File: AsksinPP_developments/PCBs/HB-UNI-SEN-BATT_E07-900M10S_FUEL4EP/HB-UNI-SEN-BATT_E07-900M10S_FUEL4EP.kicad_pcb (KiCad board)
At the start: 2 copper layers, 75 x 75 mm, 31 parts, among them J1 Conn_01x02, J10 charge, J11 ePaper connector, J2 Conn_01x02, J3 Conn_01x02, J4 Conn_01x02, J5 ISP Programmer, J6 Conn_01x04, J7 Conn_01x04, J8 Conn_01x04, J9 Conn_01x04, Q1 IRLU024N, SW1 config button

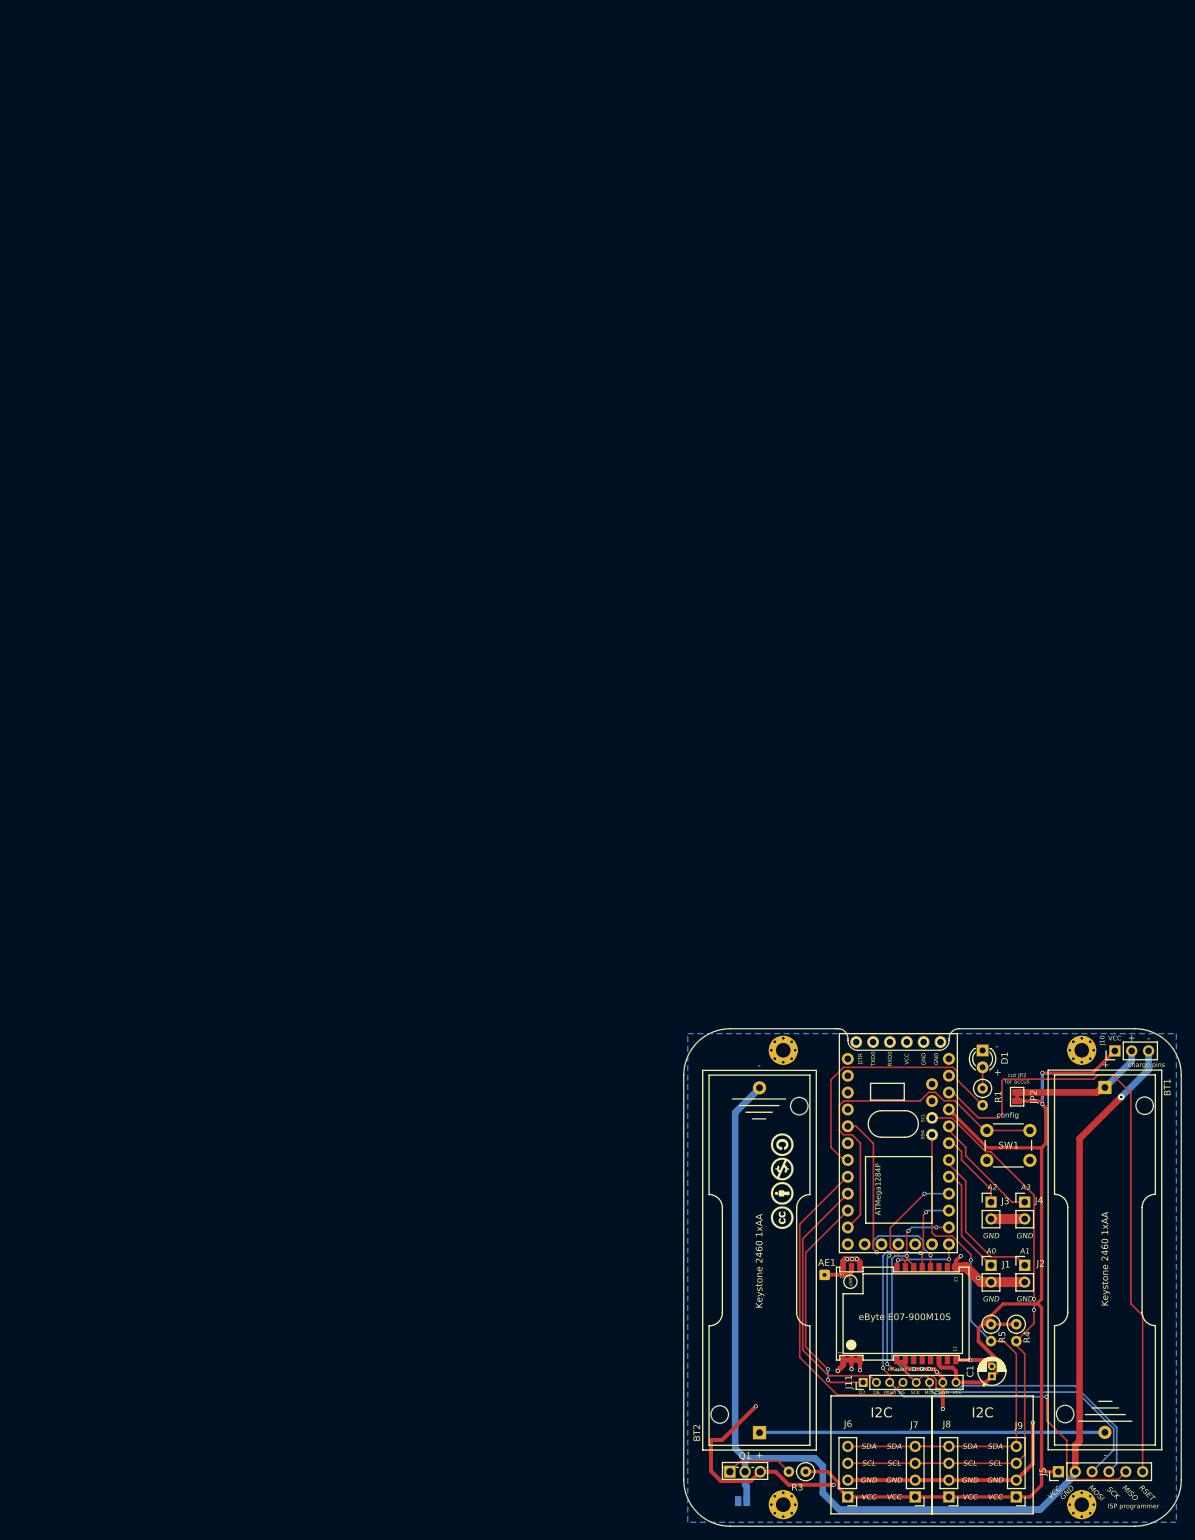
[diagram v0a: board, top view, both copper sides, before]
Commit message: PCBs: Fixes to ensure a proper production at JLCPCB, e.g. corrections of origins, rotations of assembled ICs etc.
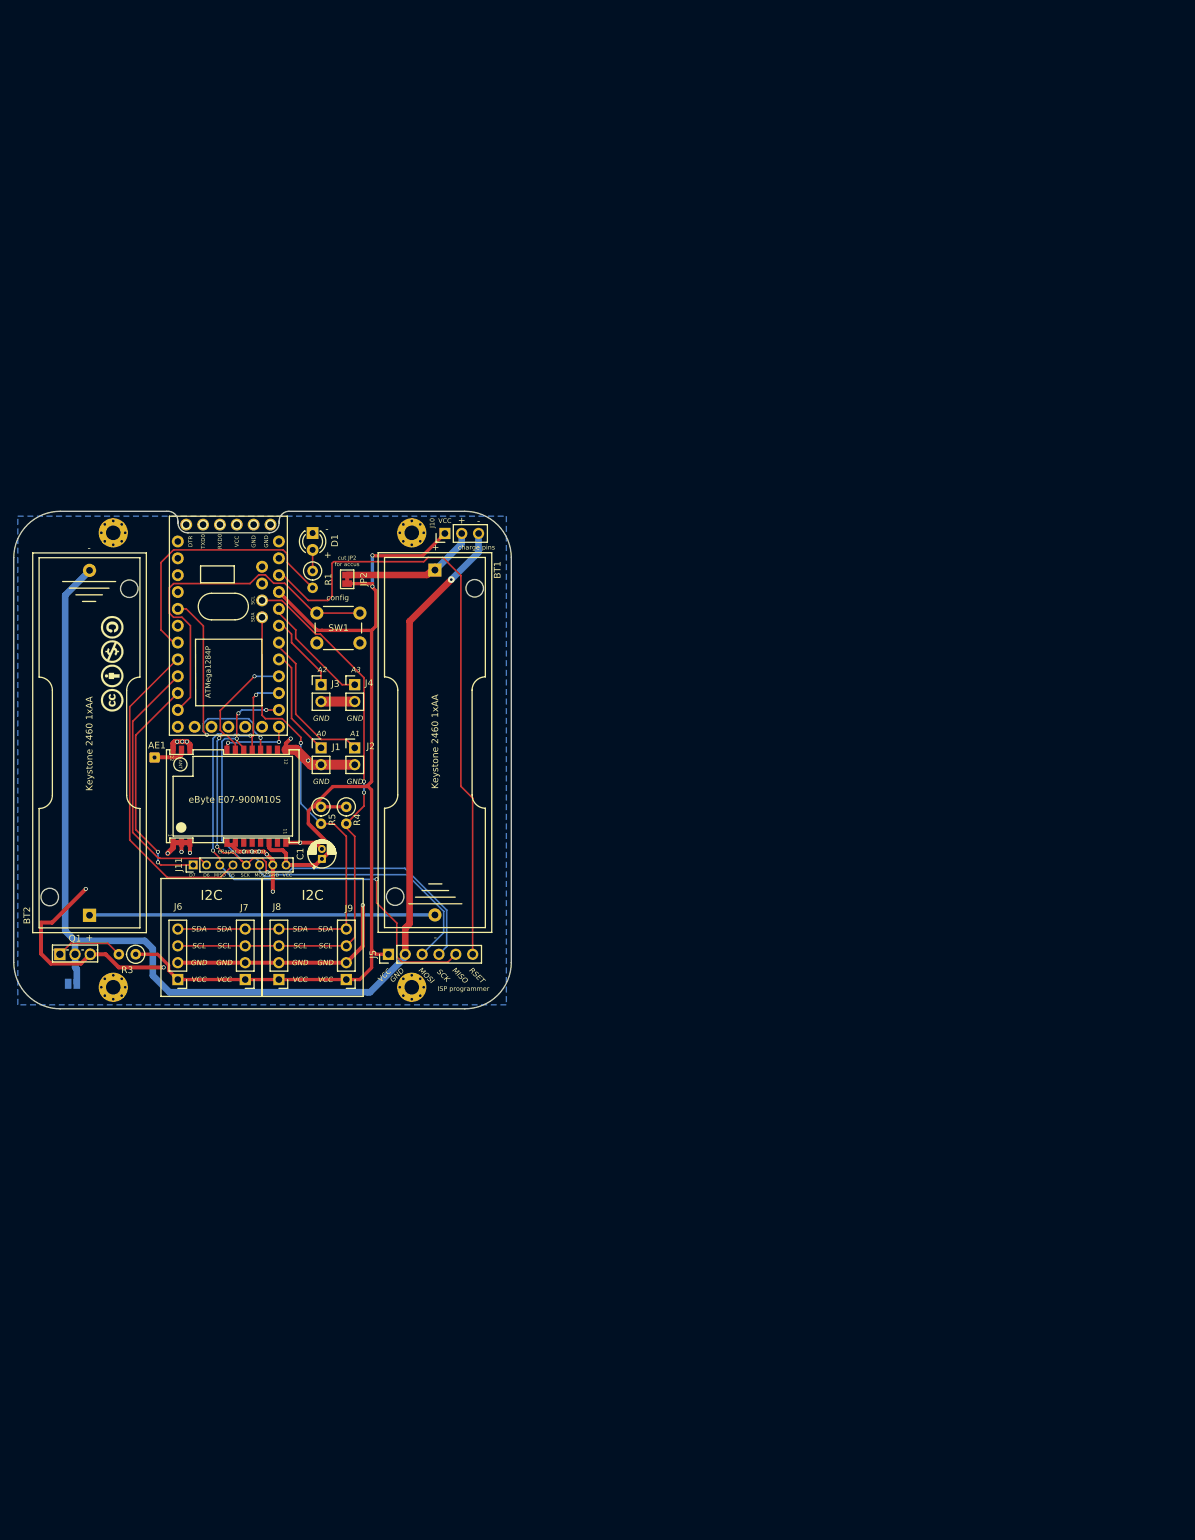
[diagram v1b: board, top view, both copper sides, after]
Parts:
- moved C1 127.6 mm to (46.4, 52.4)
- moved J11 127.6 mm to (27.0, 53.3)
- moved D1 127.6 mm to (45.0, 3.28)
- moved R1 127.6 mm to (45.0, 8.99)
- moved AE1 127.6 mm to (21.2, 37.1)
- moved BT1 127.6 mm to (63.5, 8.86)
- moved BT2 127.6 mm to (11.4, 60.9)
- moved H1 127.6 mm to (15.0, 3.25)
- moved H2 127.6 mm to (60.0, 3.25)
- moved H3 127.6 mm to (15.0, 71.8)
- moved H4 127.6 mm to (60.0, 71.8)
- moved J1 127.6 mm to (46.3, 35.7)
- moved J10 127.6 mm to (65.0, 3.34)
- moved J2 127.6 mm to (51.4, 35.7)
- moved J3 127.6 mm to (46.3, 26.1)
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
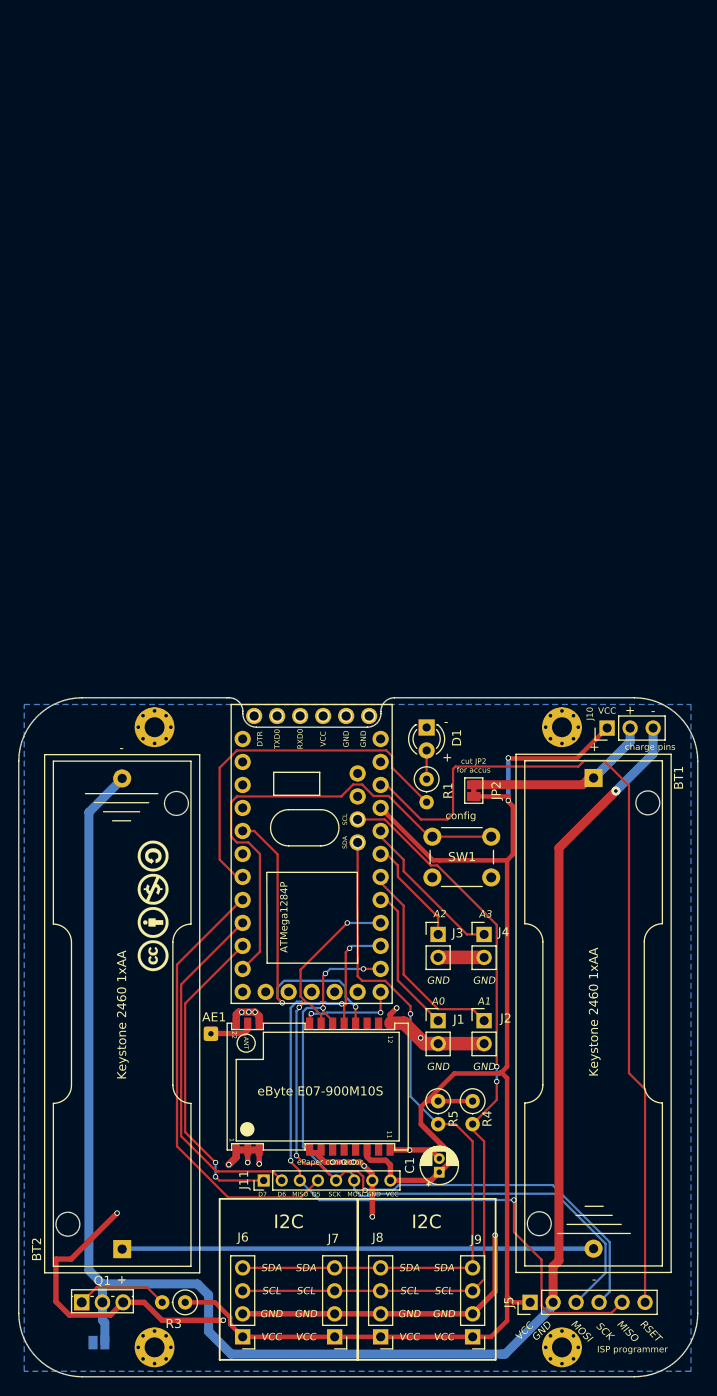
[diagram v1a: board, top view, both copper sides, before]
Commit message: PCBs: moved origin to lower left corner in order to fit to JLCPCB's scheme
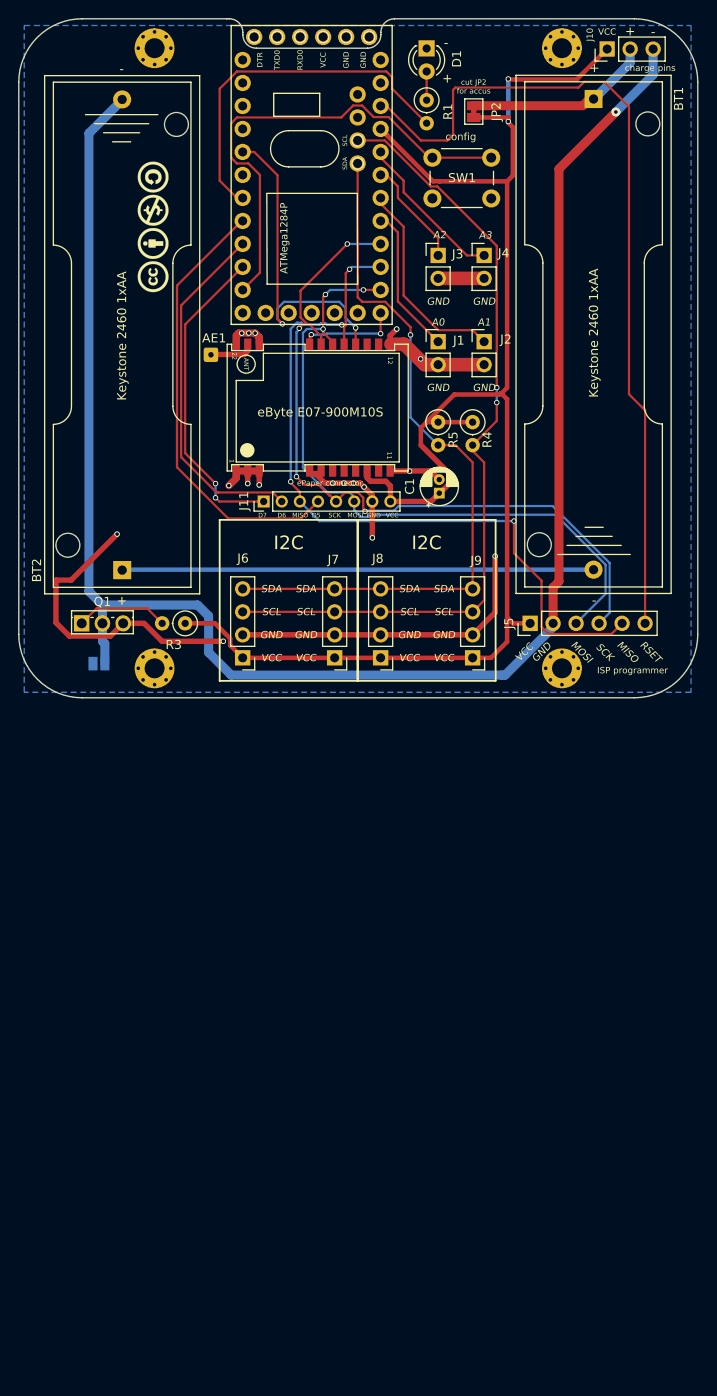
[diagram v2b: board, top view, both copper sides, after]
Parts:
- moved AE1 75.0 mm to (21.2, -37.9)
- moved BT1 75.0 mm to (63.5, -66.1)
- moved BT2 75.0 mm to (11.4, -14.1)
- moved C1 75.0 mm to (46.4, -22.6)
- moved D1 75.0 mm to (45.0, -71.7)
- moved H1 75.0 mm to (15.0, -71.8)
- moved H2 75.0 mm to (60.0, -71.8)
- moved H3 75.0 mm to (15.0, -3.25)
- moved H4 75.0 mm to (60.0, -3.25)
- moved J1 75.0 mm to (46.3, -39.3)
- moved J10 75.0 mm to (65.0, -71.7)
- moved J11 75.0 mm to (27.0, -21.7)
- moved J2 75.0 mm to (51.4, -39.3)
- moved J3 75.0 mm to (46.3, -48.9)
- moved J4 75.0 mm to (51.4, -48.9)
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
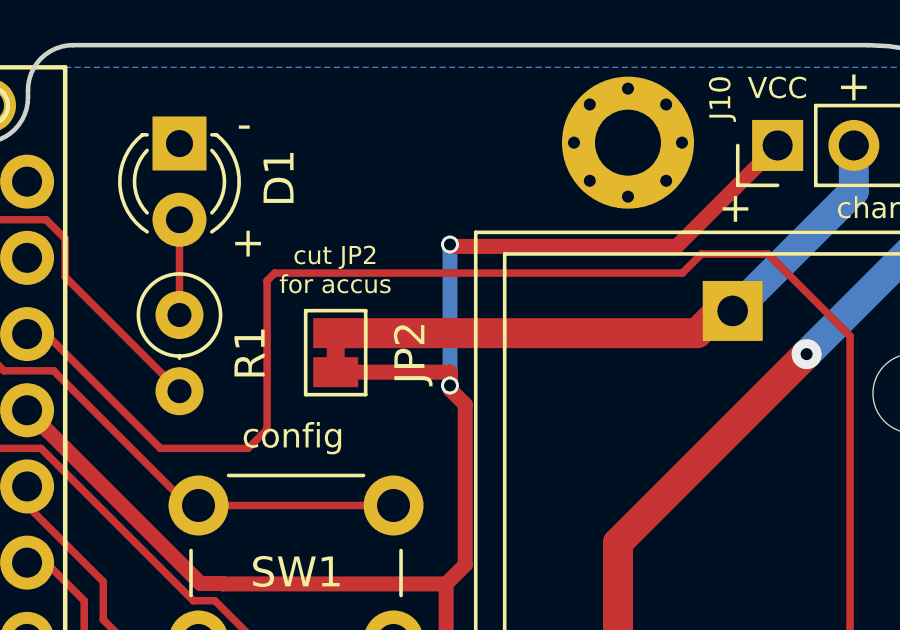
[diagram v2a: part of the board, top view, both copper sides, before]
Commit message: PCBs/HB-UNI-SEN-BATT_E07-868MS10_FUEL4EP: migration to KiCAD 8
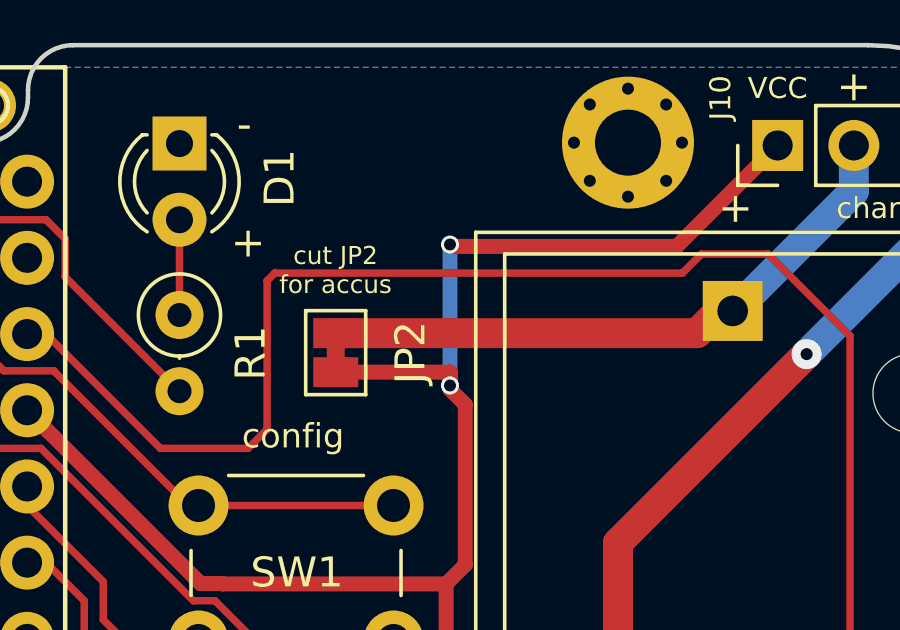
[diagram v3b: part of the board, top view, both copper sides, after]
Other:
- board text added: "Version 1.1 - 09/2024 (KiCAD 8)"
- board text removed: "Version 1.0 - 07/2023 (KiCAD 6)"

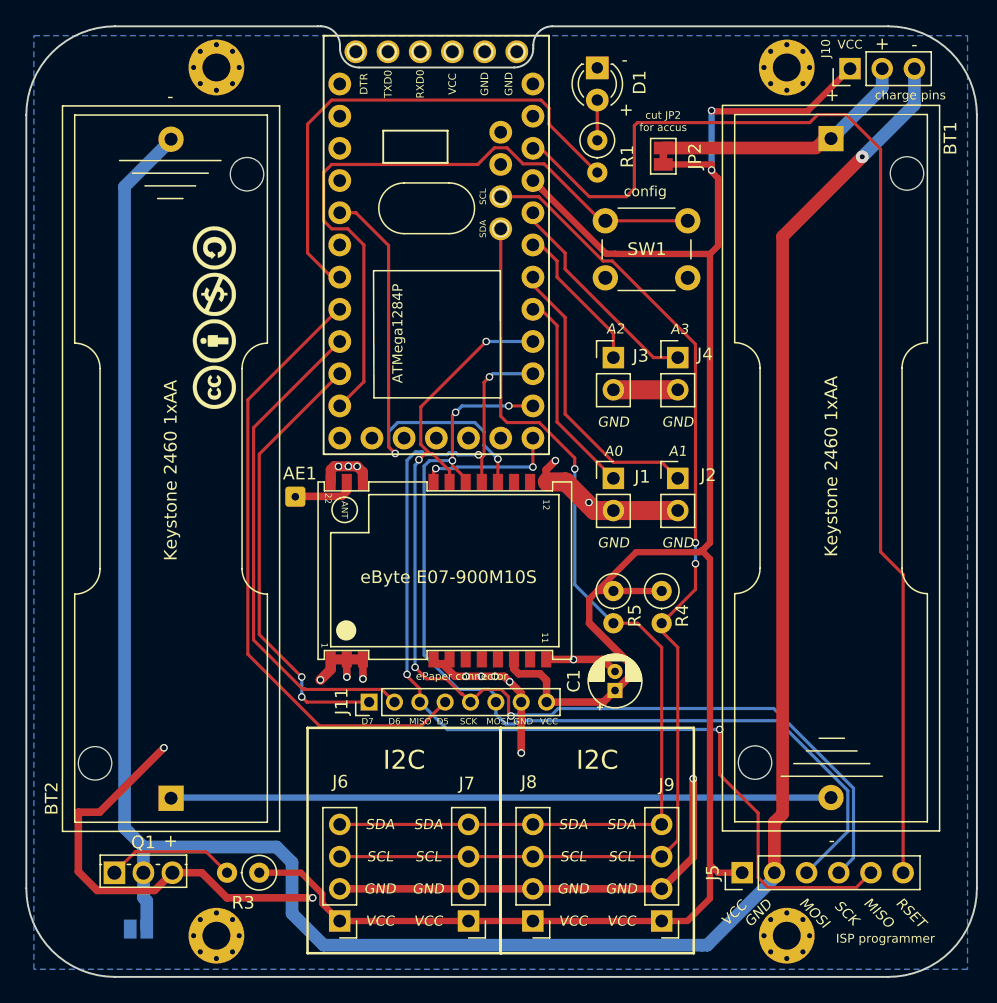
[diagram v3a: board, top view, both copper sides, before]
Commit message: update of PCBs/HB-UNI-SEN-BATT_E07-868MS10_FUEL4EP, PCBs/HB-UNI-SEN-BATT_E07-900M10S_FUEL4EP, and PCBs/HB-UNI-SEN-BATT_E07-900MM10S_FUEL4EP to support HB_Pro_Mini_ATMEGA1284P_FUEL4EP
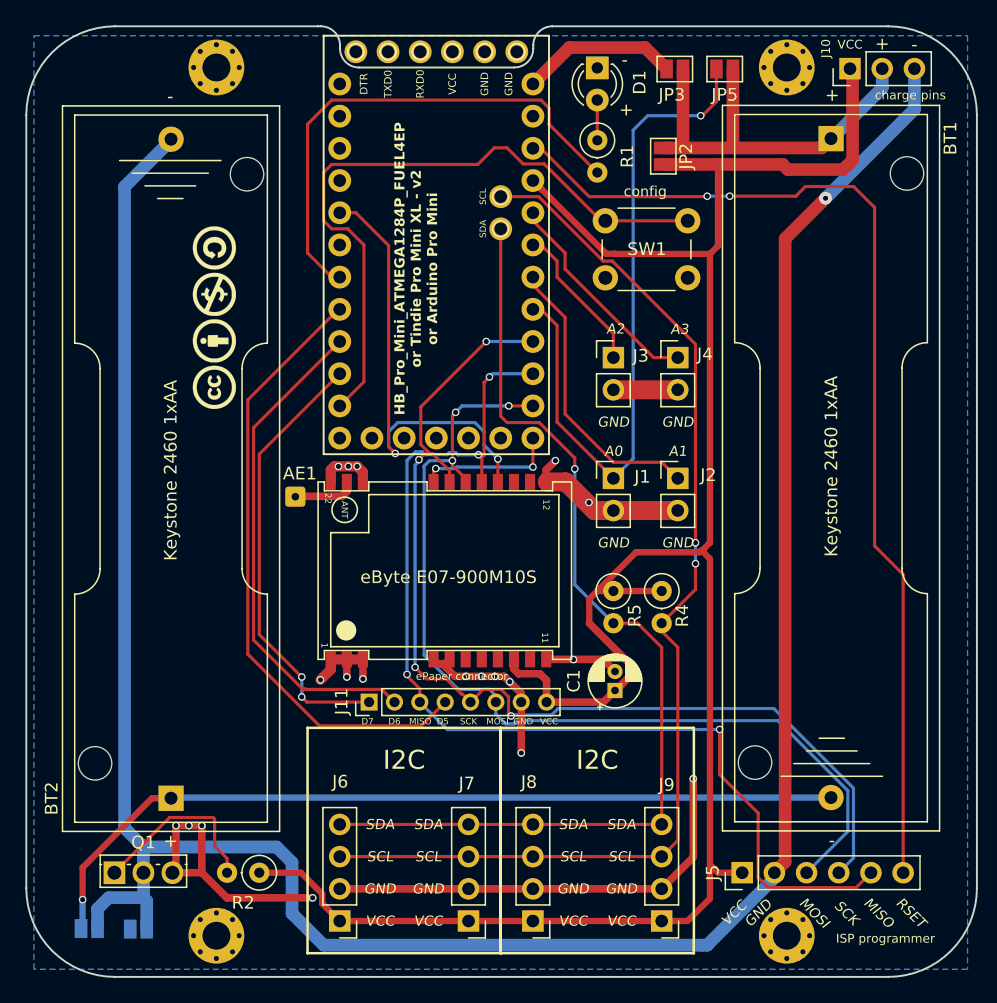
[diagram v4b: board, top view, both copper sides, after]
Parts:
- removed R3: 100K, Resistor_THT:R_Axial_DIN0207_L6.3mm_D2.5mm_P2.54mm_Vertical
- added JP3: internal boost, Jumper:SolderJumper-2_P1.3mm_Open_Pad1.0x1.5mm, F.Cu at (51.2, -71.6)
- added JP4: no BT2 battery, FUEL4EP:SolderJumper-2_P1.3mm_Open_Pad1.0x1.5mm, F.Cu at (4.97, -3.81)
- added JP5: battery voltage measurement, Jumper:SolderJumper-2_P1.3mm_Open_Pad1.0x1.5mm, F.Cu at (55.1, -71.6)
- added R2: 100K, Resistor_THT:R_Axial_DIN0207_L6.3mm_D2.5mm_P2.54mm_Vertical, F.Cu at (18.4, -8.22)
- JP2: value cut for accus -> battery supply; footprint Jumper:SolderJumper-2_P1.3mm_Bridged_Pad1.0x1.5mm -> Jumper:SolderJumper-2_P1.3mm_Open_Pad1.0x1.5mm
- Module2: value Tindie_Pro_Mini_XL_V2 -> HB_Pro_Mini_ATMEGA1284P_FUEL4EP; footprint FUEL4EP:Tindie_ArduinoProMiniXL_1284P_V2 -> FUEL4EP:HB_Pro_Mini_ATMEGA1284P_FUEL4EP
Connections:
- Module2 pad 1A: unconnected-(Module2-VCC-Pad1A) -> /V_ACCU
- Module2 pad 1E: unconnected-(Module2-VCC-Pad1E) -> /SCL
- Module2 pad 2E: GND -> /SDA
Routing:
- net /A0: track 15.7 -> 53.9 mm, vias 0 -> 1
- net /conBAT: track 52.1 -> 66.0 mm, vias 0 -> 1
- net GND: track 118.6 -> 105.6 mm, vias 17 -> 19
- net /V_ACCU: track 0.00 -> 12.4 mm
- net /plusBAT: track 20.8 -> 33.2 mm
- net /RSET: track 92.9 -> 82.3 mm, vias 0 -> 2
- net /minusBAT: track 190.2 -> 195.8 mm
- net VCC: track 173.9 -> 178.6 mm, vias 2 -> 0
- net Net-(Q1-G): track 10.3 -> 14.4 mm
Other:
- board text added: "HB_Pro_Mini_ATMEGA1284P_FUEL4EP or Tindie Pro Mini XL - v2 or Arduino Pro Mini"
- board text added: "JLCJLCJLCJLC"
- board text added: "Version 1.2 - 03/2025 (KiCAD 8)"
- board text removed: "Version 1.1 - 09/2024 (KiCAD 8)"
- board text removed: "cut JP2 for accus"
